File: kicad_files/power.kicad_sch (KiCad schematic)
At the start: 21 parts, among them J8 Conn_01x02_Socket, Q1 FDMC510P-MS, SW3 SW_SPST, U11 LT1963AxST-3.3, U12 AP63205WU

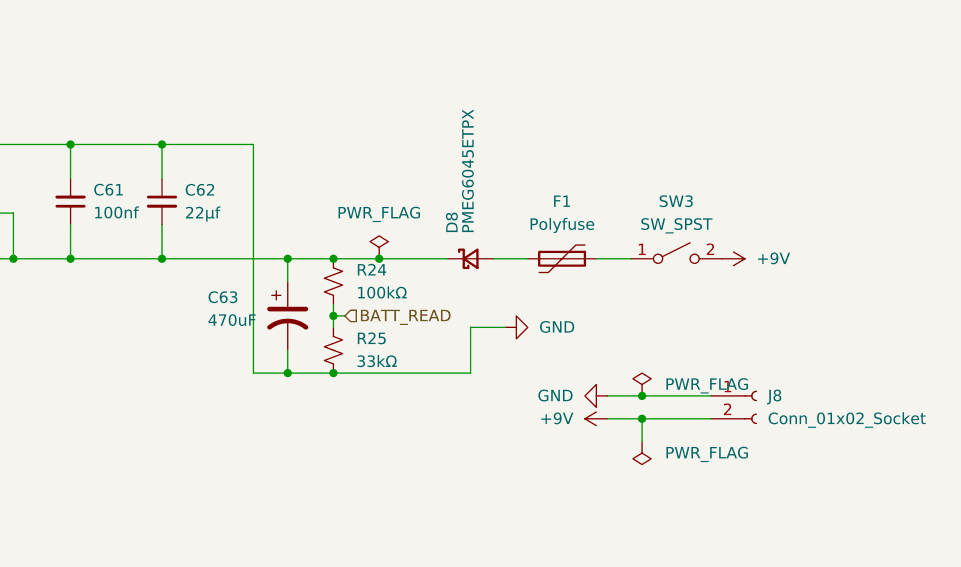
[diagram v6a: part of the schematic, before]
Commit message: Address all non-footprint DRC errors
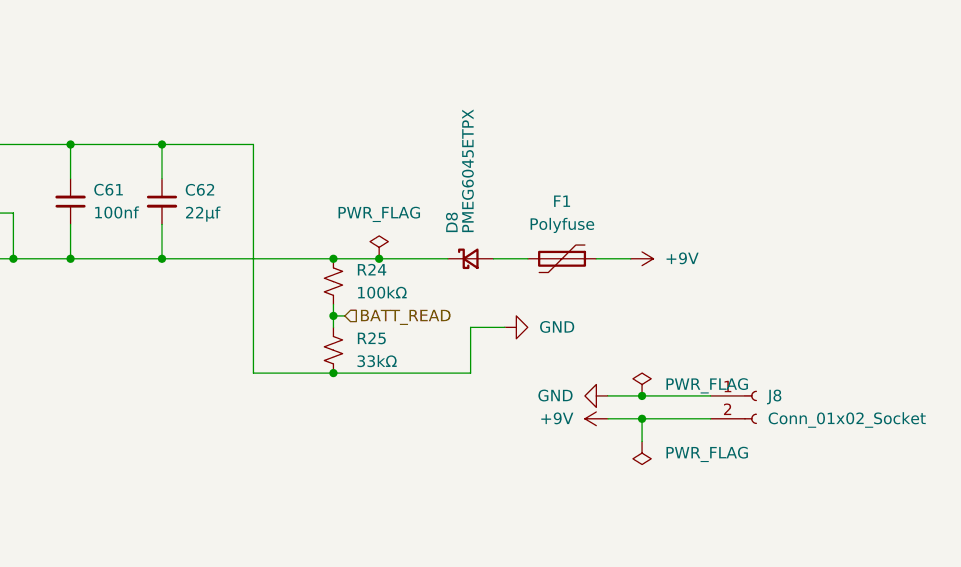
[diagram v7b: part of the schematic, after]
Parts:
- removed C63: 470uF, Capacitor_SMD:C_Elec_8x10.2, symbol Device:C_Polarized_US
- removed SW3: SW_SPST, symbol Switch:SW_SPST
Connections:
- net +9V: now also F1.1
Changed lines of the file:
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@@
 	(paper "A4")
 	(junction
-		(at 172.72 134.62)
-		(diameter 0)
-		(color 0 0 0 0)
-	)
-	(junction
 		(at 177.8 134.62)
 		(diameter 0)
@@
 	)
 	(junction
-		(at 172.72 147.32)
-		(diameter 0)
-		(color 0 0 0 0)
-	)
-	(junction
 		(at 40.64 46.99)
 		(diameter 0)
@@
 	(wire
 		(pts
-			(xy 158.75 134.62) (xy 172.72 134.62)
+			(xy 158.75 134.62) (xy 177.8 134.62)
 		)
 		(stroke
@@
 	(wire
 		(pts
-			(xy 172.72 134.62) (xy 177.8 134.62)
-		)
-		(stroke
-			(width 0)
-			(type default)
-		)
-	)
-	(wire
-		(pts
 			(xy 142.24 129.54) (xy 142.24 134.62)
 		)
@@
 	(wire
 		(pts
-			(xy 172.72 147.32) (xy 177.8 147.32)
-		)
-		(stroke
-			(width 0)
-			(type default)
-		)
-	)
-	(wire
-		(pts
 			(xy 105.41 132.08) (xy 116.84 132.08)
 		)
@@
 	(wire
 		(pts
-			(xy 172.72 134.62) (xy 172.72 137.16)
-		)
-		(stroke
-			(width 0)
-			(type default)
-		)
-	)
-	(wire
-		(pts
 			(xy 40.64 139.7) (xy 40.64 152.4)
 		)
@@
 	(wire
 		(pts
-			(xy 168.91 147.32) (xy 172.72 147.32)
+			(xy 168.91 147.32) (xy 177.8 147.32)
 		)
 		(stroke
@@
 	(wire
 		(pts
-			(xy 172.72 144.78) (xy 172.72 147.32)
-		)
-		(stroke
-			(width 0)
-			(type default)
-		)
-	)
-	(wire
-		(pts
 			(xy 158.75 130.81) (xy 158.75 134.62)
 		)
@@
 	(symbol
 		(lib_id "power:+9V")
-		(at 220.98 134.62 270)
+		(at 210.82 134.62 270)
 		(unit 1)
 		(body_style 1)
@@
 		(fields_autoplaced yes)
 		(property "Reference" "#PWR091"
-			(at 217.17 134.62 0)
+			(at 207.01 134.62 0)
 			(hide yes)
 			(show_name no)
@@
 		)
 		(property "Value" "+9V"
-			(at 224.79 134.6199 90)
+			(at 214.63 134.6199 90)
 			(show_name no)
 			(do_not_autoplace no)
@@
 		)
 		(property "Footprint" ""
-			(at 220.98 134.62 0)
+			(at 210.82 134.62 0)
 			(hide yes)
 			(show_name no)
@@
 		)
 		(property "Datasheet" ""
-			(at 220.98 134.62 0)
+			(at 210.82 134.62 0)
 			(hide yes)
 			(show_name no)
@@
 		)
 		(property "Description" "Power symbol creates a global label with name \"+9V\""
-			(at 220.98 134.62 0)
+			(at 210.82 134.62 0)
 			(hide yes)
 			(show_name no)
@@
 	)
 	(symbol
-		(lib_id "Device:C_Polarized_US")
-		(at 172.72 140.97 0)
-		(unit 1)
-		(body_style 1)
-		(exclude_from_sim no)
-		(in_bom yes)
-		(on_board yes)
-		(in_pos_files yes)
-		(dnp no)
-		(property "Reference" "C63"
-			(at 163.83 138.938 0)
-			(show_name no)
-			(do_not_autoplace no)
-			(effects
-				(font
-					(size 1.27 1.27)
-				)
-				(justify left)
-			)
-		)
-		(property "Value" "470uF"
-			(at 163.83 141.478 0)
-			(show_name no)
-			(do_not_autoplace no)
-			(effects
-				(font
-					(size 1.27 1.27)
-				)
-				(justify left)
-			)
-		)
-		(property "Footprint" "Capacitor_SMD:C_Elec_8x10.2"
-			(at 172.72 140.97 0)
-			(hide yes)
-			(show_name no)
-			(do_not_autoplace no)
-			(effects
-				(font
-					(size 1.27 1.27)
-				)
-			)
-		)
-		(property "Datasheet" ""
-			(at 172.72 140.97 0)
-			(hide yes)
-			(show_name no)
-			(do_not_autoplace no)
-			(effects
-				(font
-					(size 1.27 1.27)
-				)
-			)
-		)
-		(property "Description" "Polarized capacitor, US symbol"
-			(at 172.72 140.97 0)
-			(hide yes)
-			(show_name no)
-			(do_not_autoplace no)
-			(effects
-				(font
-					(size 1.27 1.27)
-				)
-			)
-		)
-		(pin "2"
-		)
-		(pin "1"
-		)
-		(instances
-			(project "versorlite"
-				(path "/1a230af0-0a74-48f7-8607-b087121dda49/31c1824a-552d-4de4-ae9b-4526af07be04"
-					(reference "C63")
-					(unit 1)
-				)
-			)
-		)
-	)
-	(symbol
 		(lib_id "Device:C_Small")
 		(at 45.72 100.33 90)
@@
 					(unit 1)
 				)
-			)
-		)
-	)
-	(symbol
-		(lib_id "Switch:SW_SPST")
-		(at 215.9 134.62 0)
-		(unit 1)
-		(body_style 1)
-		(exclude_from_sim no)
-		(in_bom yes)
-		(on_board yes)
-		(in_pos_files yes)
-		(dnp no)
-		(fields_autoplaced yes)
-		(property "Reference" "SW3"
-			(at 215.9 128.27 0)
-			(show_name no)
-			(do_not_autoplace no)
-			(effects
-				(font
-					(size 1.27 1.27)
-				)
-			)
-		)
-		(property "Value" "SW_SPST"
-			(at 215.9 130.81 0)
-			(show_name no)
-			(do_not_autoplace no)
-			(effects
-				(font
-					(size 1.27 1.27)
-				)
-			)
-		)
-		(property "Footprint" ""
-			(at 215.9 134.62 0)
-			(hide yes)
-			(show_name no)
-			(do_not_autoplace no)
-			(effects
-				(font
-					(size 1.27 1.27)
-				)
-			)
-		)
-		(property "Datasheet" ""
-			(at 215.9 134.62 0)
-			(hide yes)
-			(show_name no)
-			(do_not_autoplace no)
-			(effects
-				(font
-					(size 1.27 1.27)
-				)
-			)
-		)
-		(property "Description" "Single Pole Single Throw (SPST) switch"
-			(at 215.9 134.62 0)
-			(hide yes)
-			(show_name no)
-			(do_not_autoplace no)
-			(effects
-				(font
-					(size 1.27 1.27)
-				)
-			)
-		)
-		(pin "1"
-		)
-		(pin "2"
-		)
-		(instances
-			(project "versorlite"
-				(path "/1a230af0-0a74-48f7-8607-b087121dda49/31c1824a-552d-4de4-ae9b-4526af07be04"
-					(reference "SW3")
-					(unit 1)
-				)

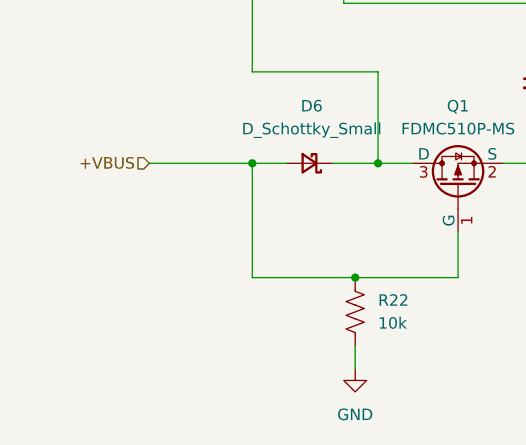
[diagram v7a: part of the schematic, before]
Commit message: add ideal diode
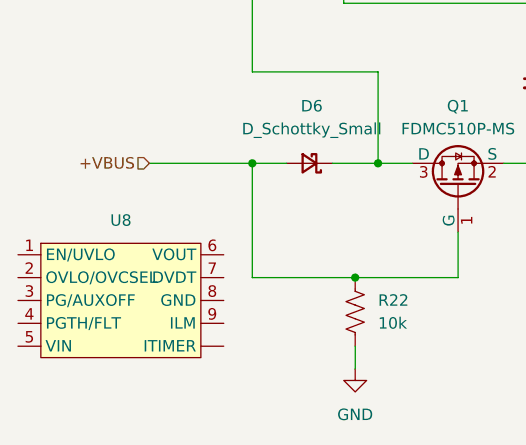
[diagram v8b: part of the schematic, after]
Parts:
- added U8: (no value), footprints:IC_TPS25974ARPWR, symbol Power_Management:TPS25947
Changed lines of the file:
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@@
+	)
+	(symbol
+		(lib_id "Power_Management:TPS25947")
+		(at 26.035 154.94 0)
+		(unit 1)
+		(body_style 1)
+		(exclude_from_sim no)
+		(in_bom yes)
+		(on_board yes)
+		(in_pos_files yes)
+		(dnp no)
+		(fields_autoplaced yes)
+		(property "Reference" "U8"
+			(at 26.035 146.05 0)
+			(show_name no)
+			(do_not_autoplace no)
+			(effects
+				(font
+					(size 1.27 1.27)
+				)
+			)
+		)
+		(property "Value" ""
+			(at 26.035 154.94 0)
+			(show_name no)
+			(do_not_autoplace no)
+			(effects
+				(font
+					(size 1.27 1.27)
+				)
+			)
+		)
+		(property "Footprint" "footprints:IC_TPS25974ARPWR"
+			(at 26.035 154.94 0)
+			(hide yes)
+			(show_name no)
+			(do_not_autoplace no)
+			(effects
+				(font
+					(size 1.27 1.27)
+				)
+			)
+		)
+		(property "Datasheet" ""
+			(at 26.035 154.94 0)
+			(hide yes)
+			(show_name no)
+			(do_not_autoplace no)
+			(effects
+				(font
+					(size 1.27 1.27)
+				)
+			)
+		)
+		(property "Description" ""
+			(at 26.035 154.94 0)
+			(hide yes)
+			(show_name no)
+			(do_not_autoplace no)
+			(effects
+				(font
+					(size 1.27 1.27)
+				)
+			)
+		)
+		(pin "5"
+		)
+		(pin "6"
+		)
+		(pin "7"
+		)
+		(pin "8"
+		)
+		(pin ""
+		)
+		(pin "4"
+		)
+		(pin "9"
+		)
+		(pin "3"
+		)
+		(pin "1"
+		)
+		(pin "2"
+		)
+		(instances
+			(project "versorlite"
+				(path "/1a230af0-0a74-48f7-8607-b087121dda49/31c1824a-552d-4de4-ae9b-4526af07be04"
+					(reference "U8")
+					(unit 1)
+				)
+			)
+		)
 	)
 	(symbol
